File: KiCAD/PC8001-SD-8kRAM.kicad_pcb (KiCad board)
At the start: 2 copper layers, 100 x 100 mm, 46 parts, among them J1 PC-8001 ext BUS, J2 AE-microSD-LLCNV, J3 AE-RTC-4543SA-V2, J4 128k MEM CTL, Q1 2SC1815, Q2 2SA1015, Q3 2N7000, SW1 RAM SW, U1 74HC04, U2 74HC32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

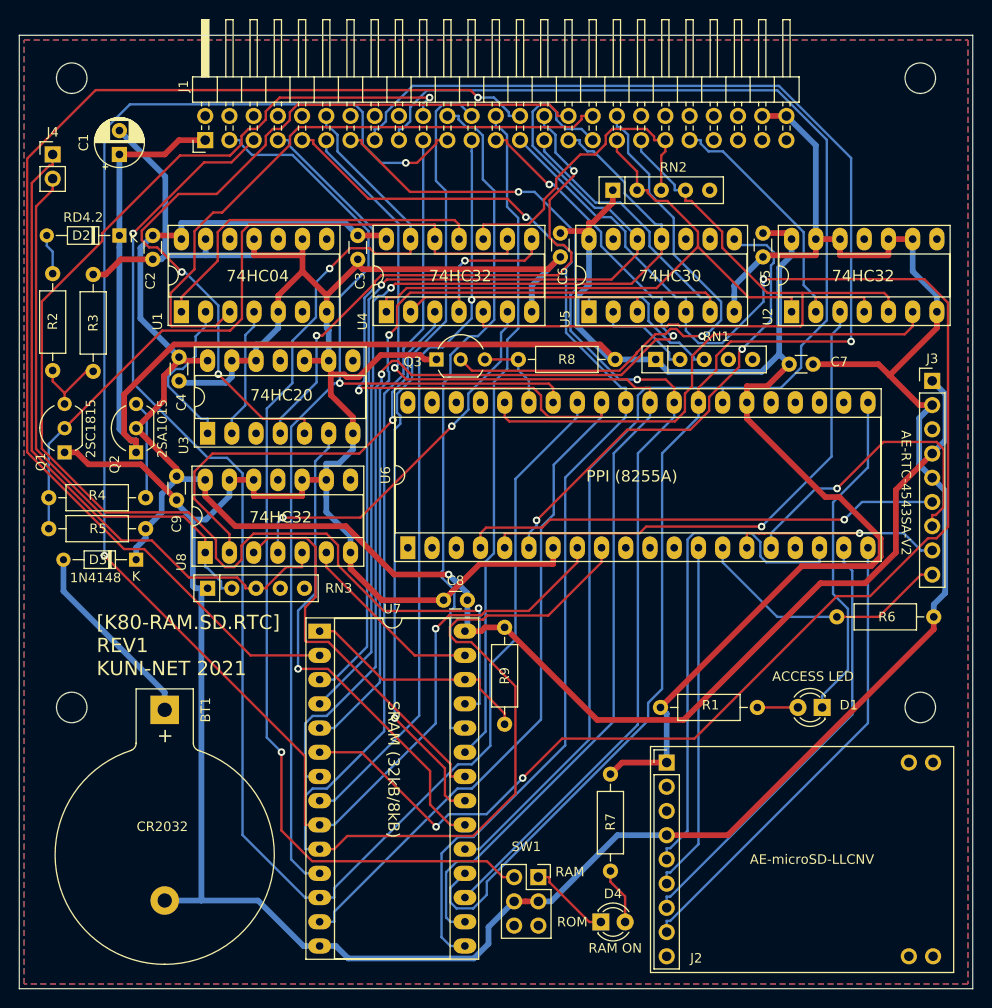
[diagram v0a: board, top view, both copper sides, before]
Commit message: ROMDS3切り離し用ジャンパパッド追加
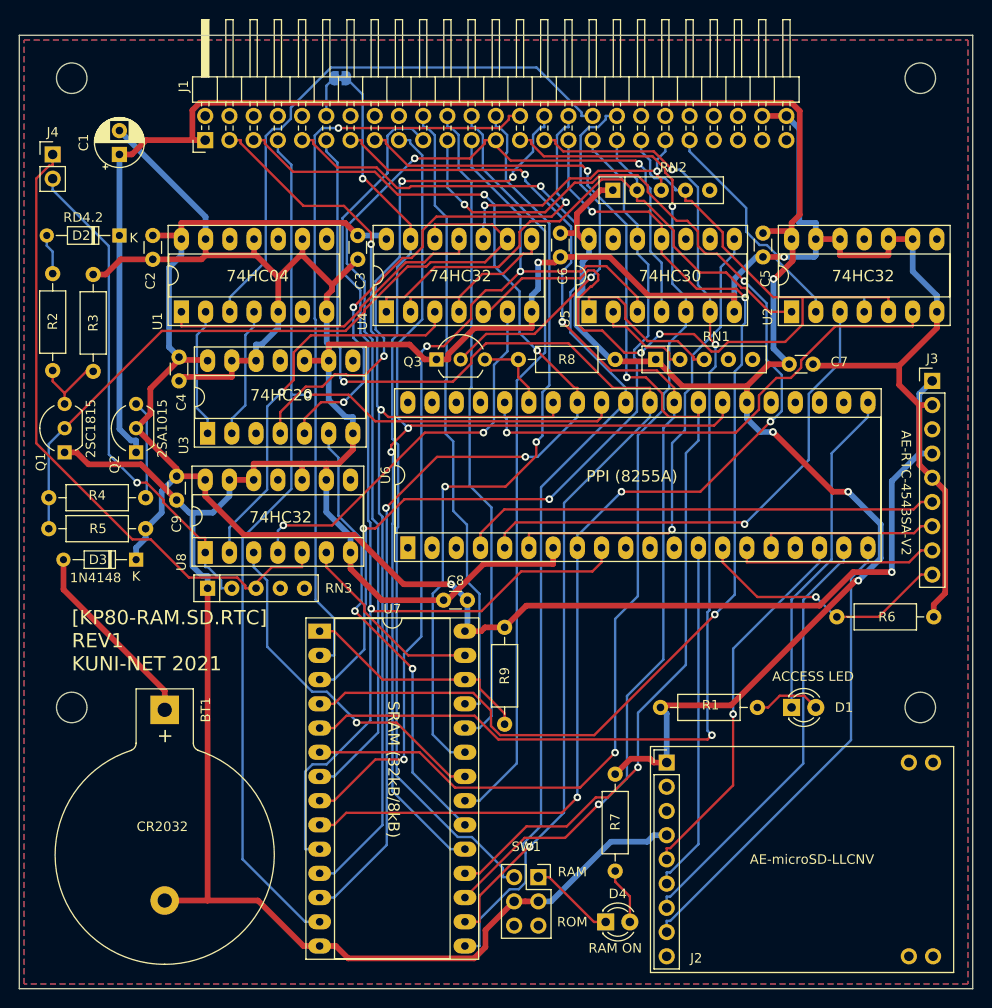
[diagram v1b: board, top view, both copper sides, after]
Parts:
- added JP1: ROM_JP, Jumper:SolderJumper-2_P1.3mm_Bridged_RoundedPad1.0x1.5mm, B.Cu at (134.7, 64.5)
- moved D1 3.21 mm to (182.0, 130.5), turned to 0 degrees
- moved D4 0.50 mm to (162.5, 153.0)
- moved R7 0.50 mm to (163.5, 137.5)
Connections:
- SW1 pad 4: /~ROMDS3 -> Net-(JP1-Pad2)
- U4 pad 13: /~ROMDS3 -> Net-(JP1-Pad2)
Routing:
- net /~ROMDS3: track 116.7 -> 4.29 mm, vias 2 -> 0
- net Net-(JP1-Pad2): track 0.00 -> 94.5 mm, vias 0 -> 1
- net /A8: track 139.3 -> 66.0 mm, vias 2 -> 0
- net /A4: track 167.5 -> 115.9 mm, vias 3 -> 2
- net /A12: track 126.3 -> 79.5 mm
- net /D6: track 165.5 -> 122.7 mm, vias 1 -> 3
- net /D1: track 161.4 -> 123.1 mm, vias 1 -> 4
- net /D7: track 151.6 -> 117.5 mm, vias 0 -> 2
- net /A0: track 146.3 -> 115.8 mm, vias 0 -> 1
- net /A1: track 171.7 -> 142.6 mm, vias 3 -> 5
- net /A14: track 83.5 -> 55.7 mm, vias 2 -> 3
- net GND: track 458.0 -> 433.2 mm, vias 0 -> 2
- net /A6: track 94.2 -> 114.6 mm, vias 1 -> 3
- net /~RESET: track 56.8 -> 38.2 mm
- net VCC: track 235.7 -> 254.3 mm, vias 0 -> 4
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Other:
- board text added: "[KP80-RAM.SD.RTC] REV1 KUNI-NET 2021"
- board text removed: "[K80-RAM.SD.RTC] REV1 KUNI-NET 2021"
